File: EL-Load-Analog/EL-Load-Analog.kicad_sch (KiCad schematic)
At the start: 10 parts, among them J1 Temp Sensor PCB, J9 Temp Sensor heatsink, Q101 TIP42C, Q4 MMBT3904

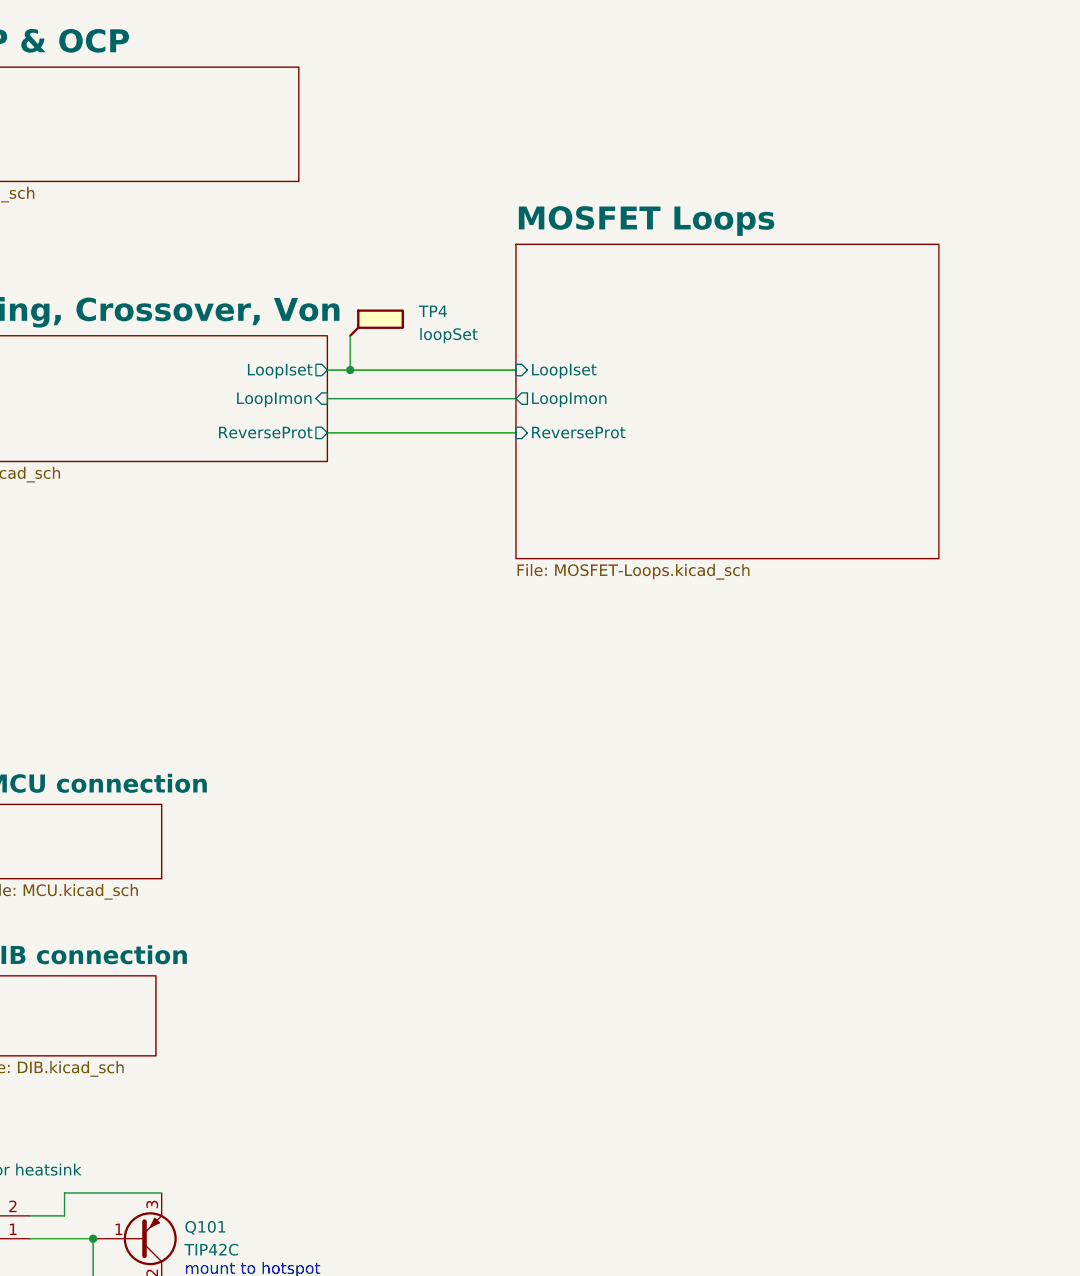
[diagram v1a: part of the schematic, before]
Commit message: v4 Analog board design. Features reverse polarity, remote sense error and new clamping circuitry.
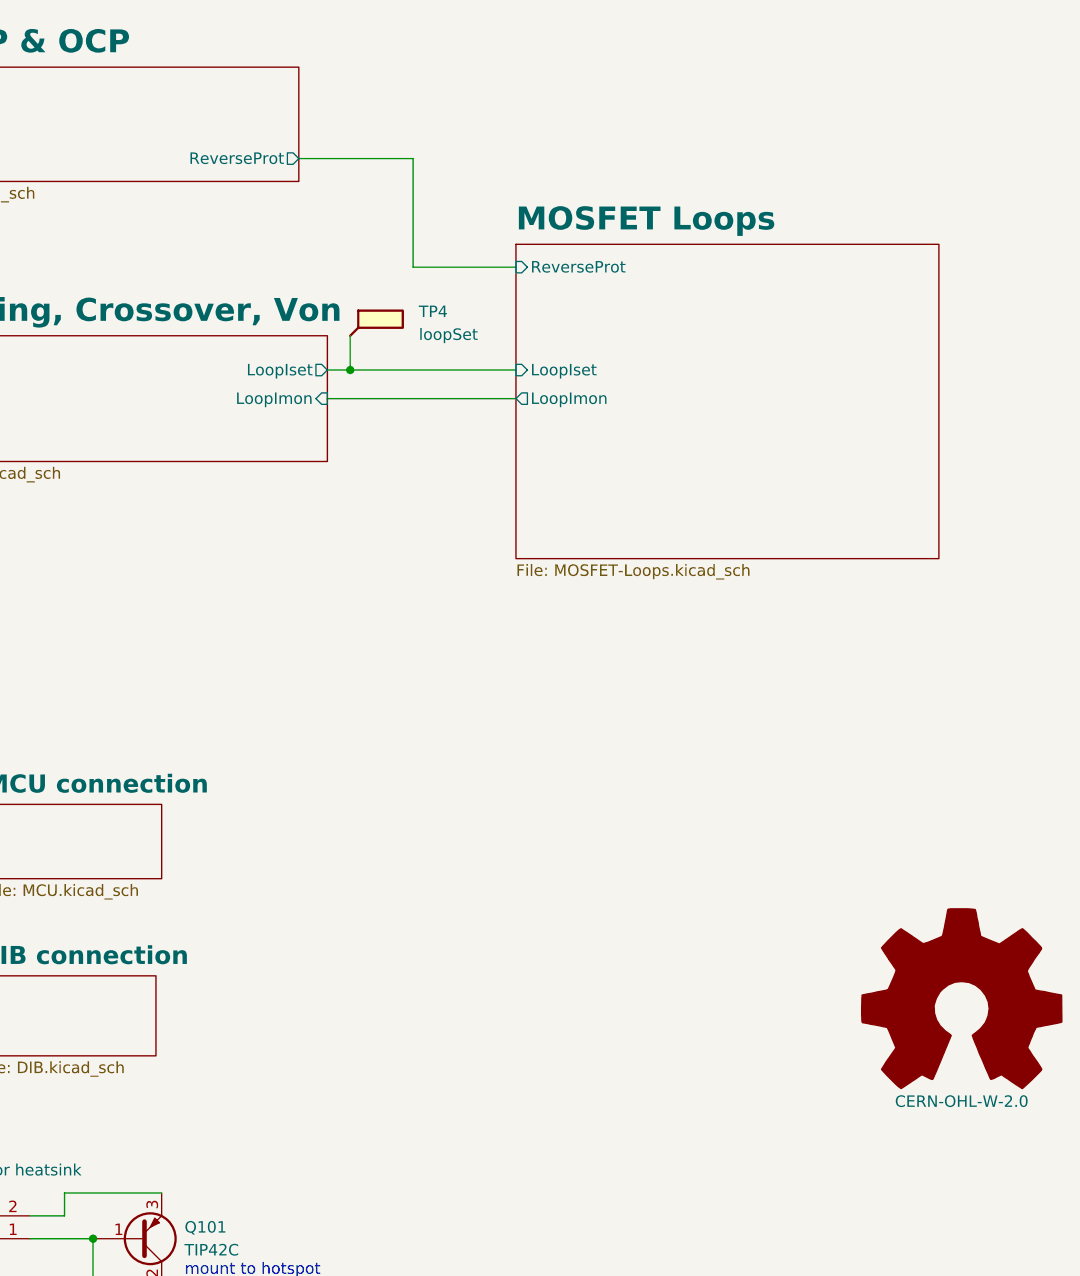
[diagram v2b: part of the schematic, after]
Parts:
- added OSHWLogo1: CERN-OHL-W-2.0, Symbol:OSHW-Logo_5.7x6mm_SilkScreen, symbol Graphic:Logo_Open_Hardware_Large
- HS102: Part Name (none) -> MH_LAM/3/150
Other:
- sheet CV, OVP & OCP ports: added ReverseProt; removed none
- sheet Monitoring, Crossover, Von ports: added none; removed ReverseProt
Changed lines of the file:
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@@
   (title_block
     (title "Electronic Load Analog Test Board")
-    (date "2024-02-06")
+    (date "2024-11-10")
     (rev "${VERSION}")
     (comment 1 "License: CERN-OHL-W-2.0")
@@
     (stroke (width 0) (type default))
   )
-  (wire (pts (xy 124.46 78.105) (xy 145.415 78.105))
+  (wire (pts (xy 133.985 59.69) (xy 133.985 47.625))
+    (stroke (width 0) (type default))
+  )
+  (wire (pts (xy 145.415 59.69) (xy 133.985 59.69))
     (stroke (width 0) (type default))
   )
@@
   )
   (wire (pts (xy 106.045 173.355) (xy 106.045 172.72))
+    (stroke (width 0) (type default))
+  )
+  (wire (pts (xy 133.985 47.625) (xy 121.285 47.625))
     (stroke (width 0) (type default))
   )
@@
     )
   )
+  (symbol (lib_id "Graphic:Logo_Open_Hardware_Large") (at 194.945 142.24 0) (unit 1)
+    (in_bom no) (on_board yes) (dnp no) (fields_autoplaced)
+    (property "Reference" "OSHWLogo1" (at 194.945 129.54 0)
+      (effects (font (size 1.27 1.27)) hide)
+    )
+    (property "Value" "CERN-OHL-W-2.0" (at 194.945 152.4 0)
+      (effects (font (size 1.27 1.27)))
+    )
+    (property "Footprint" "Symbol:OSHW-Logo_5.7x6mm_SilkScreen" (at 194.945 142.24 0)
+      (effects (font (size 1.27 1.27)) hide)
+    )
+    (property "Datasheet" "~" (at 194.945 142.24 0)
+      (effects (font (size 1.27 1.27)) hide)
+    )
+    (property "Sim.Enable" "0" (at 194.945 142.24 0)
+      (effects (font (size 1.27 1.27)) hide)
+    )
+    (instances
+      (project "EL-Load-Analog"
+        (path "/51d9228f-95b8-4f0d-bdba-83c3975c517c"
+          (reference "OSHWLogo1") (unit 1)
+        )
+      )
+    )
+  )
   (symbol (lib_id "Mechanical:MountingHole") (at 157.48 181.61 0) (unit 1)
     (in_bom no) (on_board yes) (dnp no) (fields_autoplaced)
@@
       (effects (font (size 1.27 1.27)) hide)
     )
+    (property "Part Name" "MH_LAM/3/150" (at 135.89 184.15 0)
+      (effects (font (size 1.27 1.27)) hide)
+    )
     (instances
       (project "EL-Load-Analog"
@@
       (effects (font (size 1.27 1.27)) (justify left top))
     )
+    (pin "ReverseProt" output (at 121.285 47.625 0)
+      (effects (font (size 1.27 1.27)) (justify right))
+    )
     (instances
       (project "EL-Load-Analog"
@@
       (effects (font (size 1.27 1.27)) (justify right))
     )
-    (pin "ReverseProt" output (at 124.46 78.105 0)
-      (effects (font (size 1.27 1.27)) (justify right))
-    )
     (instances
       (project "EL-Load-Analog"
@@
       (effects (font (size 1.27 1.27)) (justify left))
     )
-    (pin "ReverseProt" input (at 145.415 78.105 180)
-      (effects (font (size 1.27 1.27)) (justify left))
-    )
+    (pin "ReverseProt" input (at 145.415 59.69 180)
+      (effects (font (size 1.27 1.27)) (justify left))
+    )

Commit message: Schema changed to 4.1, PCB version E. Modified R44, Remote sense error circtuit had wrong min input.
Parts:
- OSHWLogo1: footprint Symbol:OSHW-Logo_5.7x6mm_SilkScreen -> Symbol:OSHW-Logo_7.5x8mm_SilkScreen
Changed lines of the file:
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@@
       (effects (font (size 1.27 1.27)))
     )
-    (property "Footprint" "Symbol:OSHW-Logo_5.7x6mm_SilkScreen" (at 194.945 142.24 0)
+    (property "Footprint" "Symbol:OSHW-Logo_7.5x8mm_SilkScreen" (at 194.945 142.24 0)
       (effects (font (size 1.27 1.27)) hide)
     )
